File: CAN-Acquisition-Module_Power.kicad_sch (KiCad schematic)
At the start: 39 parts, among them J1 Conn_01x04, J2 Conn_01x02, Q1 SI2318A, U1 AZ431LAN, U2 S-8581AA

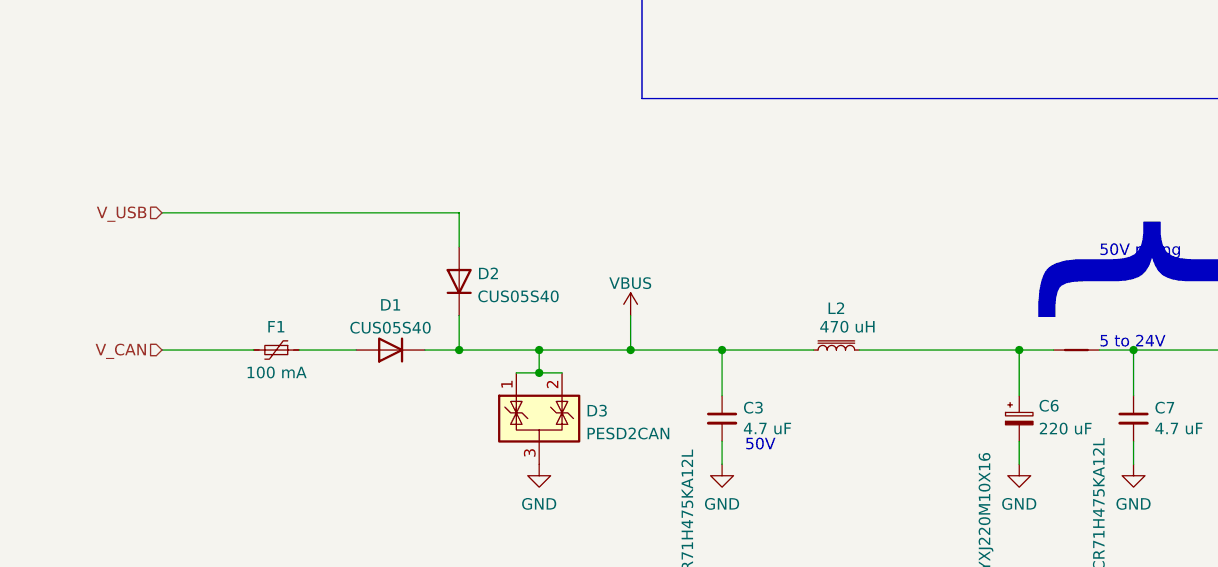
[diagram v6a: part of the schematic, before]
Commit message: Changed the node where the V_USB diode connects.
Having the V_USB go through the VBUS inductor caused the voltage to sag too low.
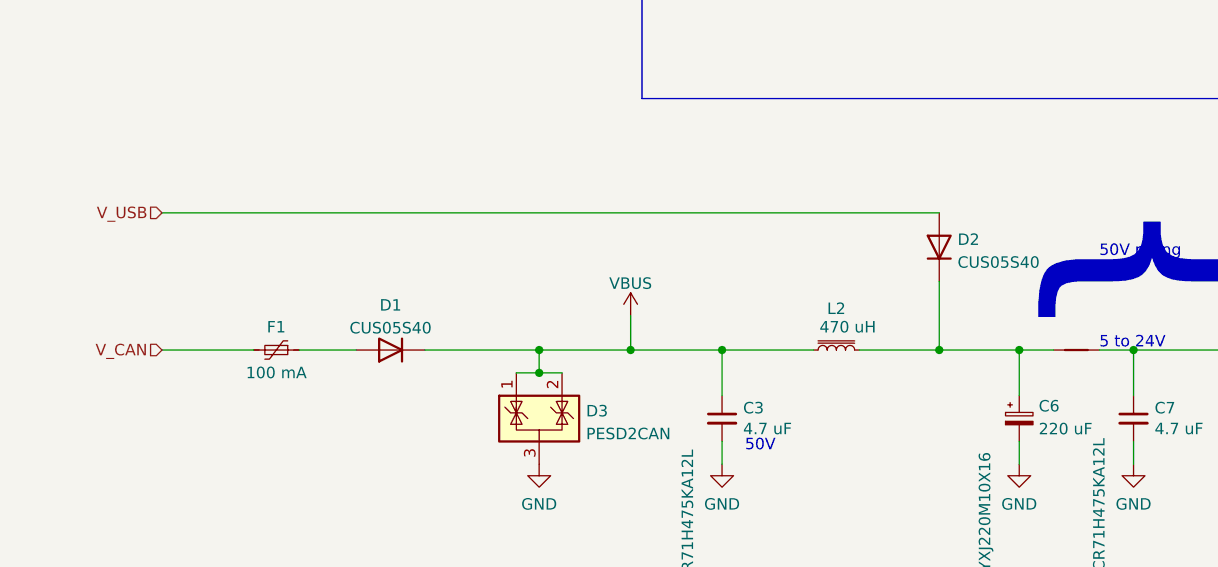
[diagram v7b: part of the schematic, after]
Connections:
- net VBUS: no longer D2.1 (K)
- net at C6.1, L2.2, NT1.1: now also D2.1 (K)
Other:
- moved on the sheet: D2
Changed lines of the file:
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@@
   (junction (at 170.18 95.25) (diameter 0) (color 0 0 0 0)
   )
-  (junction (at 82.55 95.25) (diameter 0) (color 0 0 0 0)
-  )
   (junction (at 260.35 95.25) (diameter 0) (color 0 0 0 0)
   )
@@
   (junction (at 91.44 95.25) (diameter 0) (color 0 0 0 0)
   )
+  (junction (at 135.89 95.25) (diameter 0) (color 0 0 0 0)
+  )
   (junction (at 232.41 101.6) (diameter 0) (color 0 0 0 0)
   )
@@
     (stroke (width 0) (type default) (color 0 0 0 0))
   )
-  (wire (pts (xy 127 95.25) (xy 144.78 95.25))
+  (wire (pts (xy 127 95.25) (xy 135.89 95.25))
     (stroke (width 0) (type default) (color 0 0 0 0))
   )
@@
     (stroke (width 0) (type default) (color 0 0 0 0))
   )
-  (wire (pts (xy 82.55 91.44) (xy 82.55 95.25))
-    (stroke (width 0) (type default) (color 0 0 0 0))
-  )
   (wire (pts (xy 139.7 46.99) (xy 163.83 46.99))
     (stroke (width 0) (type default) (color 0 0 0 0))
   )
-  (wire (pts (xy 78.74 95.25) (xy 82.55 95.25))
-    (stroke (width 0) (type default) (color 0 0 0 0))
-  )
   (wire (pts (xy 158.75 31.75) (xy 163.83 31.75))
     (stroke (width 0) (type default) (color 0 0 0 0))
@@
     (stroke (width 0) (type default) (color 0 0 0 0))
   )
+  (wire (pts (xy 135.89 87.63) (xy 135.89 95.25))
+    (stroke (width 0) (type default) (color 0 0 0 0))
+  )
   (polyline (pts (xy 102.87 15.24) (xy 102.87 17.78))
     (stroke (width 0) (type default) (color 0 0 0 0))
@@
     (stroke (width 0) (type default) (color 0 0 0 0))
   )
-  (wire (pts (xy 82.55 95.25) (xy 91.44 95.25))
+  (wire (pts (xy 78.74 95.25) (xy 91.44 95.25))
     (stroke (width 0) (type default) (color 0 0 0 0))
   )
@@
     (stroke (width 0) (type default) (color 0 0 0 0))
   )
-  (wire (pts (xy 82.55 80.01) (xy 82.55 83.82))
+  (wire (pts (xy 49.53 80.01) (xy 135.89 80.01))
     (stroke (width 0) (type default) (color 0 0 0 0))
   )
@@
     (stroke (width 0) (type default) (color 0 0 0 0))
   )
+  (wire (pts (xy 135.89 95.25) (xy 144.78 95.25))
+    (stroke (width 0) (type default) (color 0 0 0 0))
+  )
   (wire (pts (xy 177.8 49.53) (xy 184.15 49.53))
     (stroke (width 0) (type default) (color 0 0 0 0))
@@
   )
   (wire (pts (xy 83.82 161.29) (xy 67.31 161.29))
-    (stroke (width 0) (type default) (color 0 0 0 0))
-  )
-  (wire (pts (xy 49.53 80.01) (xy 82.55 80.01))
     (stroke (width 0) (type default) (color 0 0 0 0))
   )
@@
       (effects (font (size 1.27 1.27)) hide)
     )
-    (pin "2")
-    (pin "1")
+    (pin "1")
+    (pin "2")
     (pin "3")
   )
@@
     (pin "1")
   )
-  (symbol (lib_id "Device:D") (at 82.55 87.63 90) (unit 1)
-    (in_bom yes) (on_board yes) (fields_autoplaced)
-    (property "Reference" "D2" (id 0) (at 84.582 86.7953 90)
+  (symbol (lib_id "Device:D") (at 135.89 83.82 90) (unit 1)
+    (in_bom yes) (on_board yes) (fields_autoplaced)
+    (property "Reference" "D2" (id 0) (at 137.922 82.9853 90)
       (effects (font (size 1.27 1.27)) (justify right))
     )
-    (property "Value" "CUS05S40" (id 1) (at 84.582 89.3322 90)
+    (property "Value" "CUS05S40" (id 1) (at 137.922 85.5222 90)
       (effects (font (size 1.27 1.27)) (justify right))
     )
-    (property "Footprint" "CAN-Acquisition-Module:Toshiba_USC" (id 2) (at 82.55 87.63 0)
-      (effects (font (size 1.27 1.27)) hide)
-    )
-    (property "Datasheet" "~" (id 3) (at 82.55 87.63 0)
-      (effects (font (size 1.27 1.27)) hide)
-    )
-    (property "Mfr." "Toshiba" (id 4) (at 82.55 87.63 0)
-      (effects (font (size 1.27 1.27)) hide)
-    )
-    (property "P/N" "CUS05S40,H3F" (id 5) (at 82.55 87.63 0)
-      (effects (font (size 1.27 1.27)) hide)
-    )
+    (property "Footprint" "CAN-Acquisition-Module:Toshiba_USC" (id 2) (at 135.89 83.82 0)
+      (effects (font (size 1.27 1.27)) hide)
+    )
+    (property "Datasheet" "~" (id 3) (at 135.89 83.82 0)
+      (effects (font (size 1.27 1.27)) hide)
+    )
+    (property "Mfr." "Toshiba" (id 4) (at 135.89 83.82 0)
+      (effects (font (size 1.27 1.27)) hide)
+    )
+    (property "P/N" "CUS05S40,H3F" (id 5) (at 135.89 83.82 0)
+      (effects (font (size 1.27 1.27)) hide)
+    )
